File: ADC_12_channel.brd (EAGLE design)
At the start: 148.1 x 127 mm, 165 parts, among them IC1 LM317BD2T, IC2 LM317BD2T, K1 691131710003, K2 691101710002, K3 691101710002, K4 691101710002, K5 691101710002, K6 691101710002, K7 691101710002, K8 691101710002, K9 691101710002, U1 AD7864ASZ-1, U10 TL082D, U12 V_REG_317SMD, U2 AD7864ASZ-1, U3 TL082D, U4 TL082D, U5 TL082D, U6 TL082D, U7 TL082D, U8 TL082D, U9 TL082D, X1 QTE-040

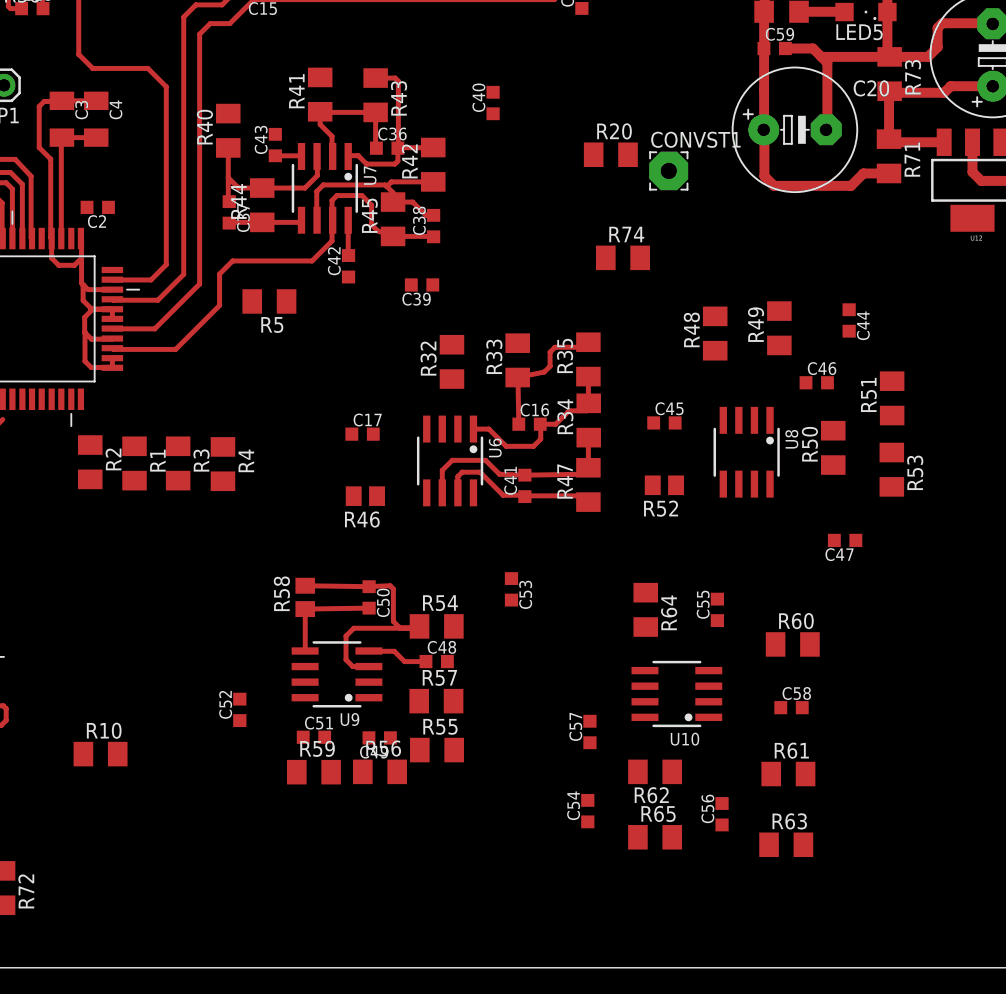
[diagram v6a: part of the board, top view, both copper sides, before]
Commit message: ADC-2 Opamp layout over
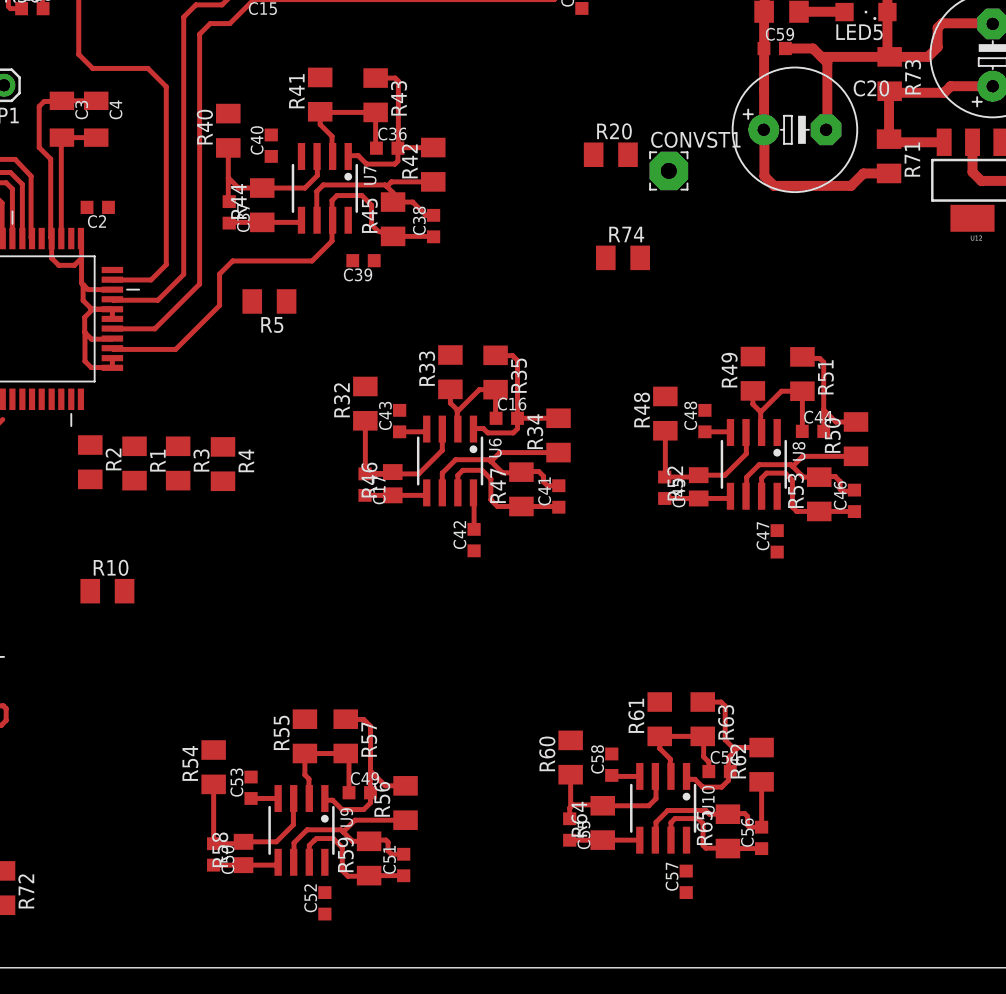
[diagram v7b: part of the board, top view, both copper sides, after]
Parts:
- moved C48 29.4 mm to (98.6, 10.1), turned to 90 degrees
- moved C53 26.7 mm to (61.5, -19.8), turned to 90 degrees
- moved C43 24.7 mm to (73.7, 10.1)
- moved C42 24.6 mm to (79.7, 0.36)
- moved C50 24.5 mm to (58.5, -25.3)
- moved C55 21.6 mm to (87.5, -23.2), turned to 270 degrees
- moved R54 21.5 mm to (58.5, -18.2), turned to 90 degrees
- moved R58 21.5 mm to (60.9, -25.2)
- moved R60 20.3 mm to (87.6, -17.4), turned to 90 degrees
- moved C40 18.4 mm to (63.2, 32.5)
- moved R64 17.7 mm to (90.2, -22.7), turned to 90 degrees
- moved C52 17.2 mm to (67.6, -29.3)
- moved C58 15.4 mm to (91.0, -18.0), turned to 90 degrees
- moved C57 14.5 mm to (97.0, -27.5)
- moved R10 13.3 mm to (49.8, -3.81)
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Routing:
- net N$77: track 0.00 -> 18.1 mm
- net N$83: track 0.00 -> 17.8 mm
- net N$81: track 0.00 -> 16.2 mm
- net N$63: track 0.00 -> 15.5 mm
- net N$89: track 0.00 -> 15.2 mm
- net N$87: track 0.00 -> 15.2 mm
- net AGND: track 121.0 -> 134.0 mm
- net N$76: track 0.00 -> 13.0 mm
- net N$88: track 0.00 -> 12.8 mm
- net ADC6: track 0.00 -> 11.8 mm
- net ADC8: track 6.39 -> 18.2 mm
- net ADC7: track 0.00 -> 11.7 mm
- net N$74: track 0.00 -> 11.1 mm
- net N$75: track 0.00 -> 10.6 mm
- net N$80: track 0.00 -> 10.5 mm
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
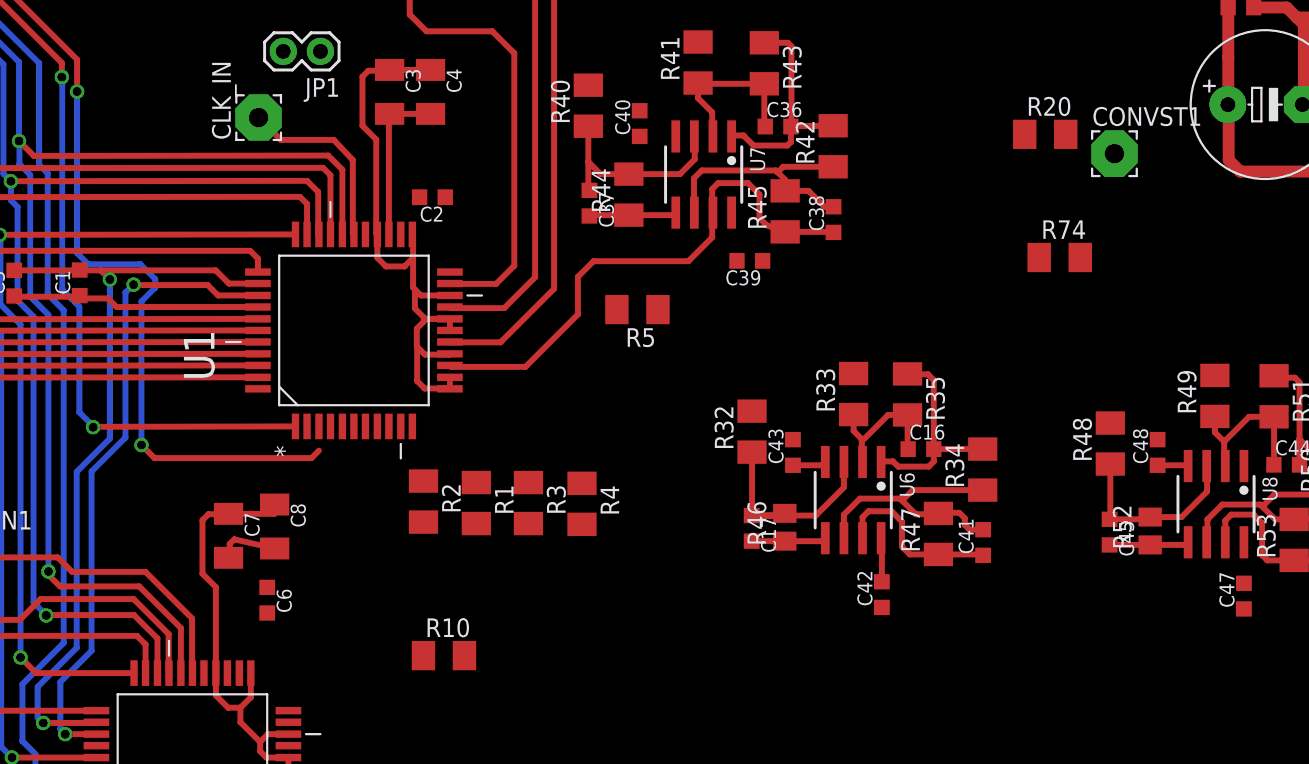
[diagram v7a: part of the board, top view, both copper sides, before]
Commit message: Routed ADC1 to header, ADC1 to ADC2
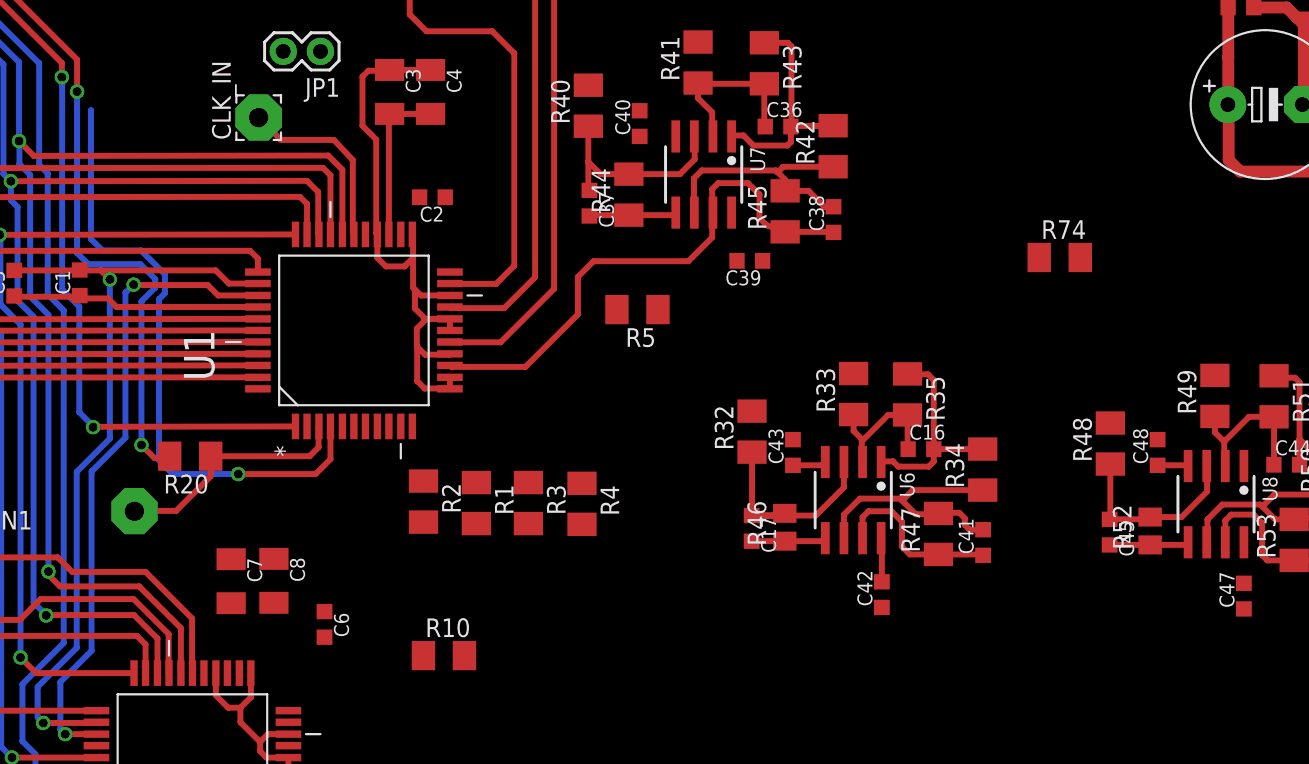
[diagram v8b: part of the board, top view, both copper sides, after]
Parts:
- moved CONVST1 71.2 mm to (28.7, 6.05), flipped to the bottom
- moved R20 62.4 mm to (32.5, 9.80), turned to 180 degrees
- moved C6 4.25 mm to (41.7, -1.68)
- moved C8 3.71 mm to (38.2, 1.30)
- moved C7 3.10 mm to (35.3, 1.27)
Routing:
- net CS2N: track 0.00 -> 42.5 mm, vias 0 -> 1
- net N$18: track 0.00 -> 16.6 mm
- net AGND: track 134.0 -> 117.5 mm
- net CONVST: track 92.4 -> 82.1 mm
- net VDD: track 15.3 -> 11.0 mm
